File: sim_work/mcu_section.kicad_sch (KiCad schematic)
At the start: 7 parts

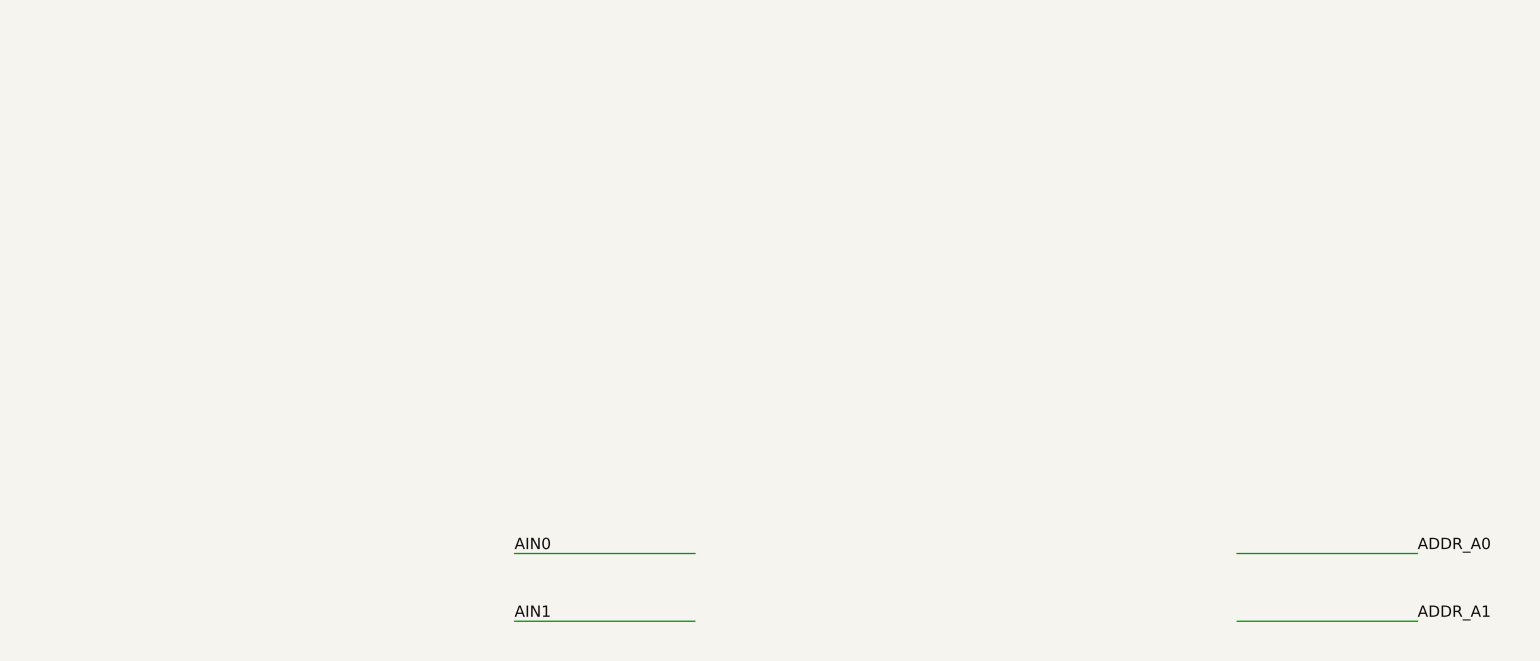
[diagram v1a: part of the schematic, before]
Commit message: Fix schematic connections, add docs and repo portability
- Input filters: R rotation=90 (horizontal), ESD diode rotations fixed,
  junction dots at cathode-signal connection, wires to GND symbols
- Relay ladder: flyback diode rotation 270->90 (K top, A bottom)
- Electrometer/Mux TIA: 4 junction dots each at T-junctions
- AD636 RMS detector: proper IC box with pin labels replaces text-only
- Oscillator blocks: D_Zener symbol, L-shaped cathode routing
- TIA blocks: title/function annotations on all 5 blocks
- New: requirements.txt, docs/oscillator_guide.md
- D_Zener.kicad_sym added to bundled symbols/
- .gitignore updated for docs/ and requirements.txt
- README updated with pip install -r requirements.txt
- PROJECT.md session 9 changelog
- SimGUI builds clean (0 errors)

Co-Authored-By: Claude Opus 4.6 <noreply@anthropic.com>
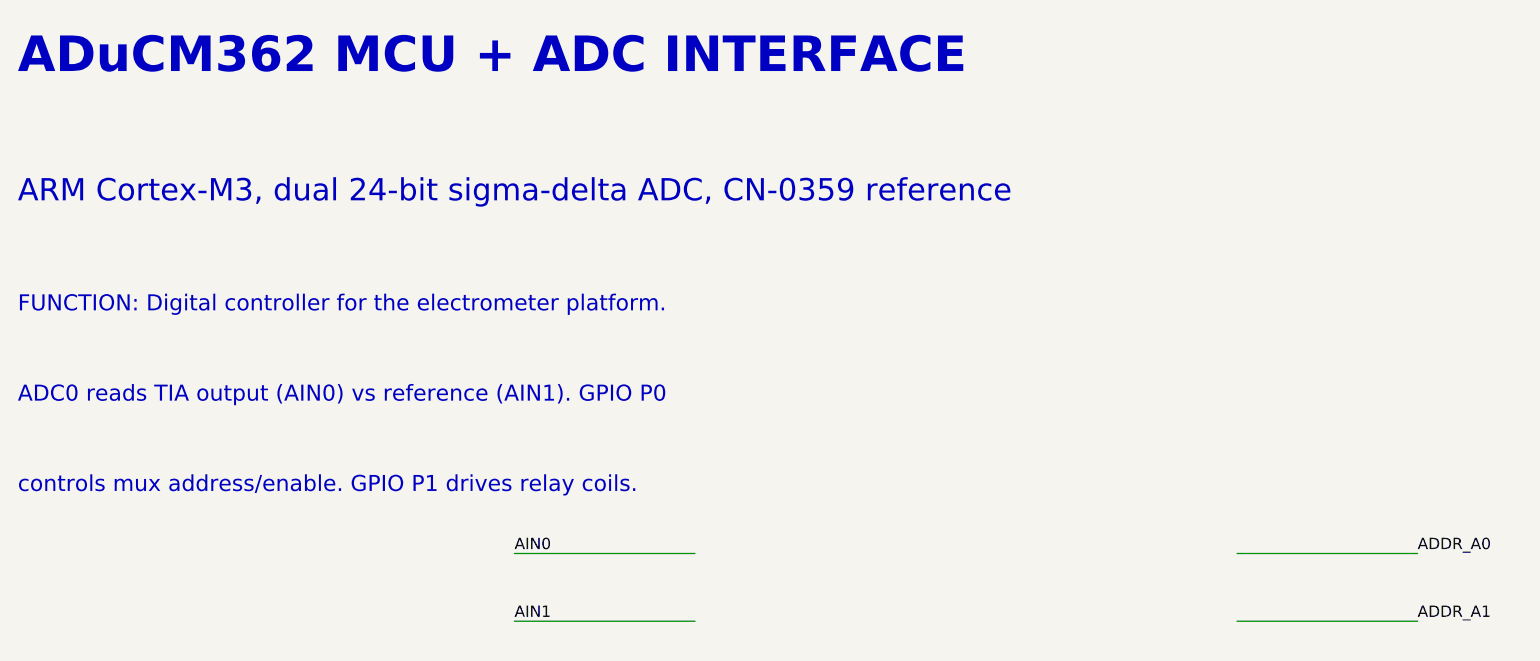
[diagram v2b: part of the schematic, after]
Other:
- note added: "ADC0 reads TIA output (AIN0) vs reference (AIN1). GPIO P0"
- note added: "ADuCM362 MCU + ADC INTERFACE"
- note added: "ARM Cortex-M3, dual 24-bit sigma-delta ADC, CN-0359 reference"
- note added: "FUNCTION: Digital controller for the electrometer platform."
- note added: "controls mux address/enable. GPIO P1 drives relay coils."
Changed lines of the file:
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@@
 		(instances
 			(project "ADuCM362 MCU + ADC Interface (CN-0359 based)"
-				(path "/beff749f-9449-4c91-8399-ab5ef36950c6"
+				(path "/e7478baf-3eed-4fd1-b65a-be1930f8506d"
 					(reference "C1")
 					(unit 1)
@@
 		(instances
 			(project "ADuCM362 MCU + ADC Interface (CN-0359 based)"
-				(path "/beff749f-9449-4c91-8399-ab5ef36950c6"
+				(path "/e7478baf-3eed-4fd1-b65a-be1930f8506d"
 					(reference "#PWR001")
 					(unit 1)
@@
 		(instances
 			(project "ADuCM362 MCU + ADC Interface (CN-0359 based)"
-				(path "/beff749f-9449-4c91-8399-ab5ef36950c6"
+				(path "/e7478baf-3eed-4fd1-b65a-be1930f8506d"
 					(reference "#PWR002")
 					(unit 1)
@@
 		(instances
 			(project "ADuCM362 MCU + ADC Interface (CN-0359 based)"
-				(path "/beff749f-9449-4c91-8399-ab5ef36950c6"
+				(path "/e7478baf-3eed-4fd1-b65a-be1930f8506d"
 					(reference "C2")
 					(unit 1)
@@
 		(instances
 			(project "ADuCM362 MCU + ADC Interface (CN-0359 based)"
-				(path "/beff749f-9449-4c91-8399-ab5ef36950c6"
+				(path "/e7478baf-3eed-4fd1-b65a-be1930f8506d"
 					(reference "#PWR003")
 					(unit 1)
@@
 		(instances
 			(project "ADuCM362 MCU + ADC Interface (CN-0359 based)"
-				(path "/beff749f-9449-4c91-8399-ab5ef36950c6"
+				(path "/e7478baf-3eed-4fd1-b65a-be1930f8506d"
 					(reference "C3")
 					(unit 1)
@@
 		(instances
 			(project "ADuCM362 MCU + ADC Interface (CN-0359 based)"
-				(path "/beff749f-9449-4c91-8399-ab5ef36950c6"
+				(path "/e7478baf-3eed-4fd1-b65a-be1930f8506d"
 					(reference "#PWR004")
 					(unit 1)
@@
 		(instances
 			(project "ADuCM362 MCU + ADC Interface (CN-0359 based)"
-				(path "/beff749f-9449-4c91-8399-ab5ef36950c6"
+				(path "/e7478baf-3eed-4fd1-b65a-be1930f8506d"
 					(reference "#PWR005")
 					(unit 1)
@@
 		(instances
 			(project "ADuCM362 MCU + ADC Interface (CN-0359 based)"
-				(path "/beff749f-9449-4c91-8399-ab5ef36950c6"
+				(path "/e7478baf-3eed-4fd1-b65a-be1930f8506d"
 					(reference "C4")
 					(unit 1)
@@
 		(instances
 			(project "ADuCM362 MCU + ADC Interface (CN-0359 based)"
-				(path "/beff749f-9449-4c91-8399-ab5ef36950c6"
+				(path "/e7478baf-3eed-4fd1-b65a-be1930f8506d"
 					(reference "#PWR006")
 					(unit 1)
@@
 		(instances
 			(project "ADuCM362 MCU + ADC Interface (CN-0359 based)"
-				(path "/beff749f-9449-4c91-8399-ab5ef36950c6"
+				(path "/e7478baf-3eed-4fd1-b65a-be1930f8506d"
 					(reference "C5")
 					(unit 1)
@@
 		(instances
 			(project "ADuCM362 MCU + ADC Interface (CN-0359 based)"
-				(path "/beff749f-9449-4c91-8399-ab5ef36950c6"
+				(path "/e7478baf-3eed-4fd1-b65a-be1930f8506d"
 					(reference "#PWR007")
 					(unit 1)
@@
 		(instances
 			(project "ADuCM362 MCU + ADC Interface (CN-0359 based)"
-				(path "/beff749f-9449-4c91-8399-ab5ef36950c6"
+				(path "/e7478baf-3eed-4fd1-b65a-be1930f8506d"
 					(reference "C6")
 					(unit 1)
@@
 		(instances
 			(project "ADuCM362 MCU + ADC Interface (CN-0359 based)"
-				(path "/beff749f-9449-4c91-8399-ab5ef36950c6"
+				(path "/e7478baf-3eed-4fd1-b65a-be1930f8506d"
 					(reference "#PWR008")
 					(unit 1)
@@
 		(instances
 			(project "ADuCM362 MCU + ADC Interface (CN-0359 based)"
-				(path "/beff749f-9449-4c91-8399-ab5ef36950c6"
+				(path "/e7478baf-3eed-4fd1-b65a-be1930f8506d"
 					(reference "C7")
 					(unit 1)
@@
 		(instances
 			(project "ADuCM362 MCU + ADC Interface (CN-0359 based)"
-				(path "/beff749f-9449-4c91-8399-ab5ef36950c6"
+				(path "/e7478baf-3eed-4fd1-b65a-be1930f8506d"
 					(reference "#PWR009")
 					(unit 1)
@@
 		)
 	)
+	(text "ADuCM362 MCU + ADC INTERFACE"
+		(exclude_from_sim no)
+		(at 20.32 15.24 0.0000)
+		(effects
+			(font
+				(size 4 4)
+				(bold yes)
+			)
+			(justify left)
+		)
+	)
+	(text "ARM Cortex-M3, dual 24-bit sigma-delta ADC, CN-0359 reference"
+		(exclude_from_sim no)
+		(at 20.32 30.48 0.0000)
+		(effects
+			(font
+				(size 2.5 2.5)
+			)
+			(justify left)
+		)
+	)
+	(text "FUNCTION: Digital controller for the electrometer platform."
+		(exclude_from_sim no)
+		(at 20.32 43.18 0.0000)
+		(effects
+			(font
+				(size 1.8 1.8)
+			)
+			(justify left)
+		)
+	)
+	(text "ADC0 reads TIA output (AIN0) vs reference (AIN1). GPIO P0"
+		(exclude_from_sim no)
+		(at 20.32 53.34 0.0000)
+		(effects
+			(font
+				(size 1.8 1.8)
+			)
+			(justify left)
+		)
+	)
+	(text "controls mux address/enable. GPIO P1 drives relay coils."
+		(exclude_from_sim no)
+		(at 20.32 63.5 0.0000)
+		(effects
+			(font
+				(size 1.8 1.8)
+			)
+			(justify left)
+		)
+	)
